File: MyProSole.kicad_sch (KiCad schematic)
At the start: 15 parts, among them J1 Conn_01x07_Socket_XIAO_ESP32C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, J2 XIAO_ESP32C3, J3 i2c-bus, J4 FSR1, J5 FSR2, J6 FSR3, J7 Conn_01x06

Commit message: Fix ERC
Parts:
- removed J4: FSR1, symbol Connector_Generic:Conn_01x02
- added J8: FSR3, symbol Connector_Generic:Conn_01x02
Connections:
- net +3.3V: no longer J5.1 (Pin_1), J6.1 (Pin_1)
- net GND: now also J5.2 (Pin_2), J6.2 (Pin_2), J8.2 (Pin_2)
- net FSR1_ADC renamed FSR1_Input
- net FSR1_Input: now also J6.1 (Pin_1); no longer J6.2 (Pin_2)
- net FSR2_ADC renamed FSR2_Input
- net FSR2_Input: now also J5.1 (Pin_1); no longer J5.2 (Pin_2)
- net FSR3_ADC renamed FSR3_Input
- net FSR3_Input: now also J8.1 (Pin_1)
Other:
- moved on the sheet: C1, D1, J1, J3, J5, J7, R1, TP1

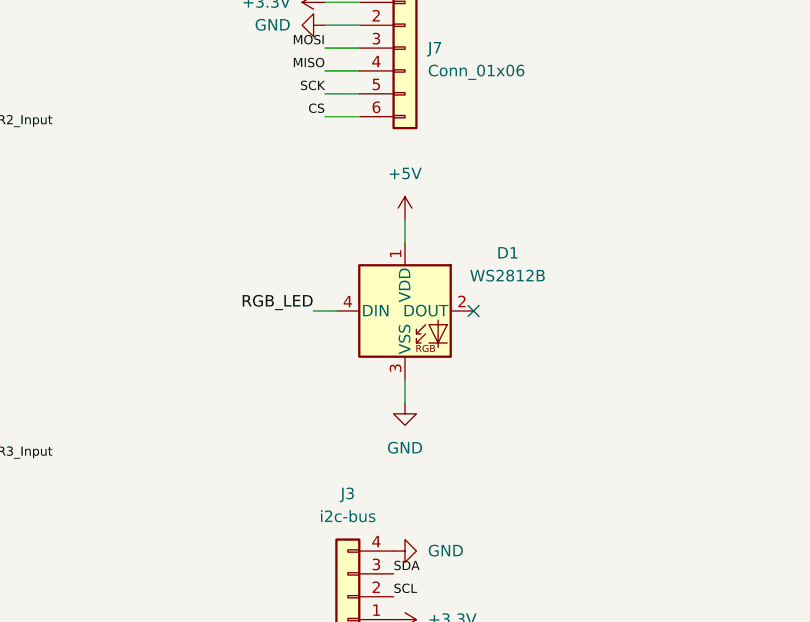
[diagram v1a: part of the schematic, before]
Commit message: Only some designed changes
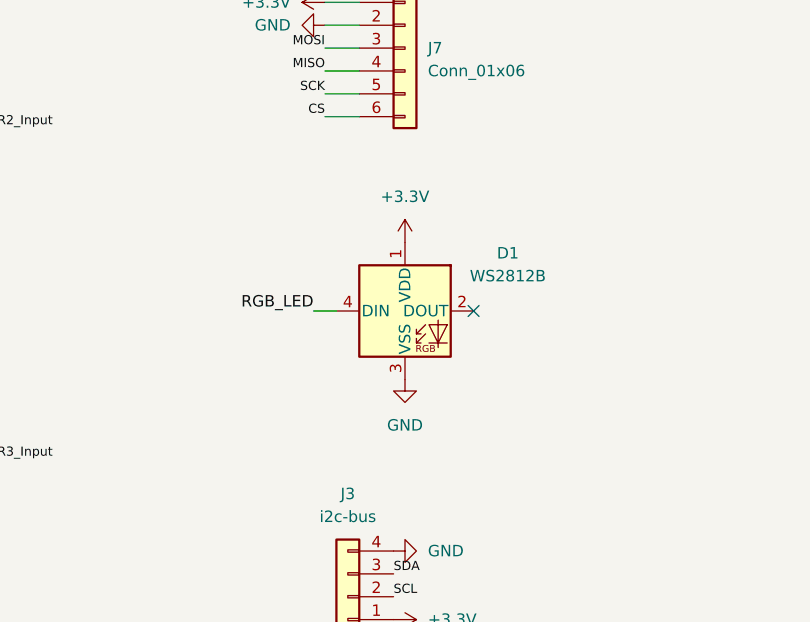
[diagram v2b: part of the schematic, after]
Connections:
- net +3.3V: now also D1.1 (VDD)
- net +5V: no longer D1.1 (VDD)
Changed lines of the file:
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@@
-	(wire
-		(pts
-			(xy 83.82 74.93) (xy 83.82 77.47)
-		)
-		(stroke
-			(width 0)
-			(type default)
-		)
-	)
 	(wire
 		(pts
@@
 		(pts
 			(xy 29.21 92.71) (xy 29.21 99.06)
-		)
-		(stroke
-			(width 0)
-			(type default)
-		)
-	)
-	(wire
-		(pts
-			(xy 83.82 92.71) (xy 83.82 95.25)
 		)
 		(stroke
@@
 	)
 	(symbol
+		(lib_id "power:+3.3V")
+		(at 83.82 77.47 0)
+		(unit 1)
+		(exclude_from_sim no)
+		(in_bom yes)
+		(on_board yes)
+		(dnp no)
+		(fields_autoplaced yes)
+		(property "Reference" "#PWR09"
+			(at 83.82 81.28 0)
+			(effects
+				(font
+					(size 1.27 1.27)
+				)
+				(hide yes)
+			)
+		)
+		(property "Value" "+3.3V"
+			(at 83.82 72.39 0)
+			(effects
+				(font
+					(size 1.27 1.27)
+				)
+			)
+		)
+		(property "Footprint" ""
+			(at 83.82 77.47 0)
+			(effects
+				(font
+					(size 1.27 1.27)
+				)
+				(hide yes)
+			)
+		)
+		(property "Datasheet" ""
+			(at 83.82 77.47 0)
+			(effects
+				(font
+					(size 1.27 1.27)
+				)
+				(hide yes)
+			)
+		)
+		(property "Description" "Power symbol creates a global label with name \"+3.3V\""
+			(at 83.82 77.47 0)
+			(effects
+				(font
+					(size 1.27 1.27)
+				)
+				(hide yes)
+			)
+		)
+		(pin "1"
+		)
+		(instances
+			(project ""
+				(path "/387d8c27-351f-4ca1-8104-be77ff5eb18f"
+					(reference "#PWR09")
+					(unit 1)
+				)
+			)
+		)
+	)
+	(symbol
 		(lib_id "Device:R_Small")
 		(at 31.75 107.95 180)
@@
 				(path "/387d8c27-351f-4ca1-8104-be77ff5eb18f"
 					(reference "R3")
-					(unit 1)
-				)
-			)
-		)
-	)
-	(symbol
-		(lib_id "power:GND")
-		(at 83.82 95.25 0)
-		(unit 1)
-		(exclude_from_sim no)
-		(in_bom yes)
-		(on_board yes)
-		(dnp no)
-		(fields_autoplaced yes)
-		(property "Reference" "#PWR011"
-			(at 83.82 101.6 0)
-			(effects
-				(font
-					(size 1.27 1.27)
-				)
-				(hide yes)
-			)
-		)
-		(property "Value" "GND"
-			(at 83.82 100.33 0)
-			(effects
-				(font
-					(size 1.27 1.27)
-				)
-			)
-		)
-		(property "Footprint" ""
-			(at 83.82 95.25 0)
-			(effects
-				(font
-					(size 1.27 1.27)
-				)
-				(hide yes)
-			)
-		)
-		(property "Datasheet" ""
-			(at 83.82 95.25 0)
-			(effects
-				(font
-					(size 1.27 1.27)
-				)
-				(hide yes)
-			)
-		)
-		(property "Description" "Power symbol creates a global label with name \"GND\" , ground"
-			(at 83.82 95.25 0)
-			(effects
-				(font
-					(size 1.27 1.27)
-				)
-				(hide yes)
-			)
-		)
-		(pin "1"
-		)
-		(instances
-			(project ""
-				(path "/387d8c27-351f-4ca1-8104-be77ff5eb18f"
-					(reference "#PWR011")
 					(unit 1)
 				)
@@
 	)
 	(symbol
-		(lib_id "power:+5V")
-		(at 83.82 74.93 0)
-		(unit 1)
-		(exclude_from_sim no)
-		(in_bom yes)
-		(on_board yes)
-		(dnp no)
-		(fields_autoplaced yes)
-		(property "Reference" "#PWR010"
-			(at 83.82 78.74 0)
-			(effects
-				(font
-					(size 1.27 1.27)
-				)
-				(hide yes)
-			)
-		)
-		(property "Value" "+5V"
-			(at 83.82 69.85 0)
-			(effects
-				(font
-					(size 1.27 1.27)
-				)
-			)
-		)
-		(property "Footprint" ""
-			(at 83.82 74.93 0)
-			(effects
-				(font
-					(size 1.27 1.27)
-				)
-				(hide yes)
-			)
-		)
-		(property "Datasheet" ""
-			(at 83.82 74.93 0)
-			(effects
-				(font
-					(size 1.27 1.27)
-				)
-				(hide yes)
-			)
-		)
-		(property "Description" "Power symbol creates a global label with name \"+5V\""
-			(at 83.82 74.93 0)
-			(effects
-				(font
-					(size 1.27 1.27)
-				)
-				(hide yes)
-			)
-		)
-		(pin "1"
-		)
-		(instances
-			(project ""
-				(path "/387d8c27-351f-4ca1-8104-be77ff5eb18f"
-					(reference "#PWR010")
-					(unit 1)
-				)
-			)
-		)
-	)
-	(symbol
 		(lib_id "MyProSoleLib:Conn_01x07_Socket_XIAO_ESP32C3_Left")
 		(at 73.66 34.29 0)
@@
 					(unit 1)
 				)
+			)
+		)
+	)
+	(symbol
+		(lib_id "power:GND")
+		(at 83.82 92.71 0)
+		(unit 1)
+		(exclude_from_sim no)
+		(in_bom yes)
+		(on_board yes)
+		(dnp no)
+		(fields_autoplaced yes)
+		(property "Reference" "#PWR010"
+			(at 83.82 99.06 0)
+			(effects
+				(font
+					(size 1.27 1.27)
+				)
+				(hide yes)
+			)
+		)
+		(property "Value" "GND"
+			(at 83.82 97.79 0)
+			(effects
+				(font
+					(size 1.27 1.27)
+				)
+			)
+		)
+		(property "Footprint" ""
+			(at 83.82 92.71 0)
+			(effects
+				(font
+					(size 1.27 1.27)
+				)
+				(hide yes)
+			)
+		)
+		(property "Datasheet" ""
+			(at 83.82 92.71 0)
+			(effects
+				(font
+					(size 1.27 1.27)
+				)
+				(hide yes)
+			)
+		)
+		(property "Description" "Power symbol creates a global label with name \"GND\" , ground"
+			(at 83.82 92.71 0)
+			(effects
+				(font
+					(size 1.27 1.27)
+				)
+				(hide yes)
+			)
+		)
+		(pin "1"
+		)
+		(instances
+			(project ""
+				(path "/387d8c27-351f-4ca1-8104-be77ff5eb18f"
+					(reference "#PWR010")
+					(unit 1)
+				)

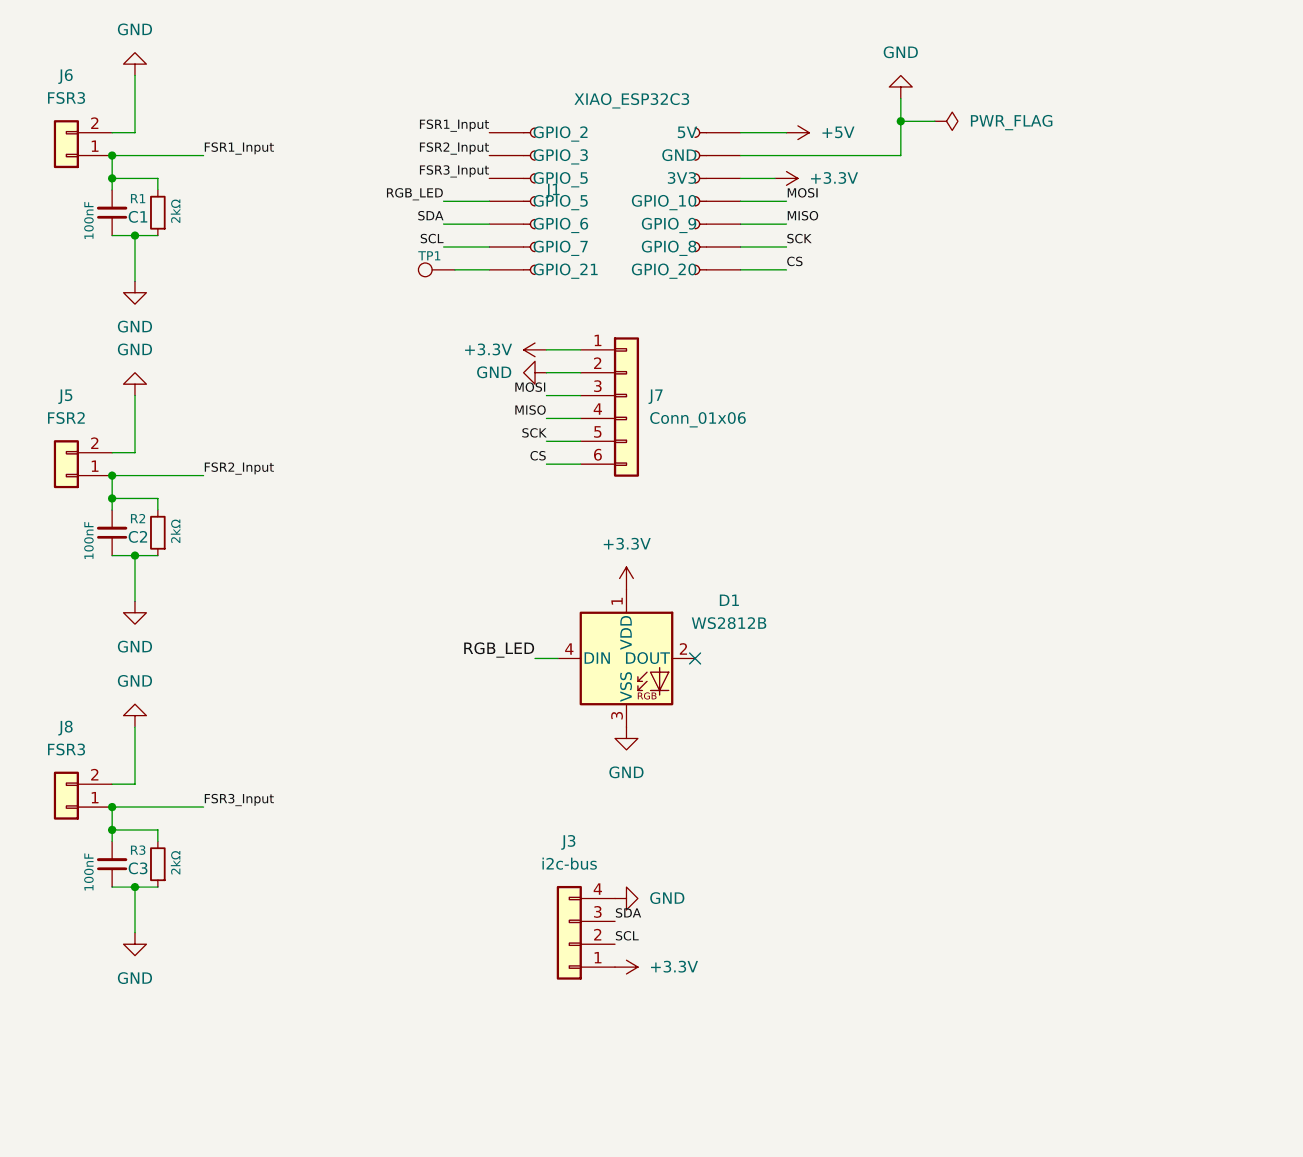
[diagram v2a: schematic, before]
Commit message: Added 5V led, Helper Socket for SD_Card & Footprints Added
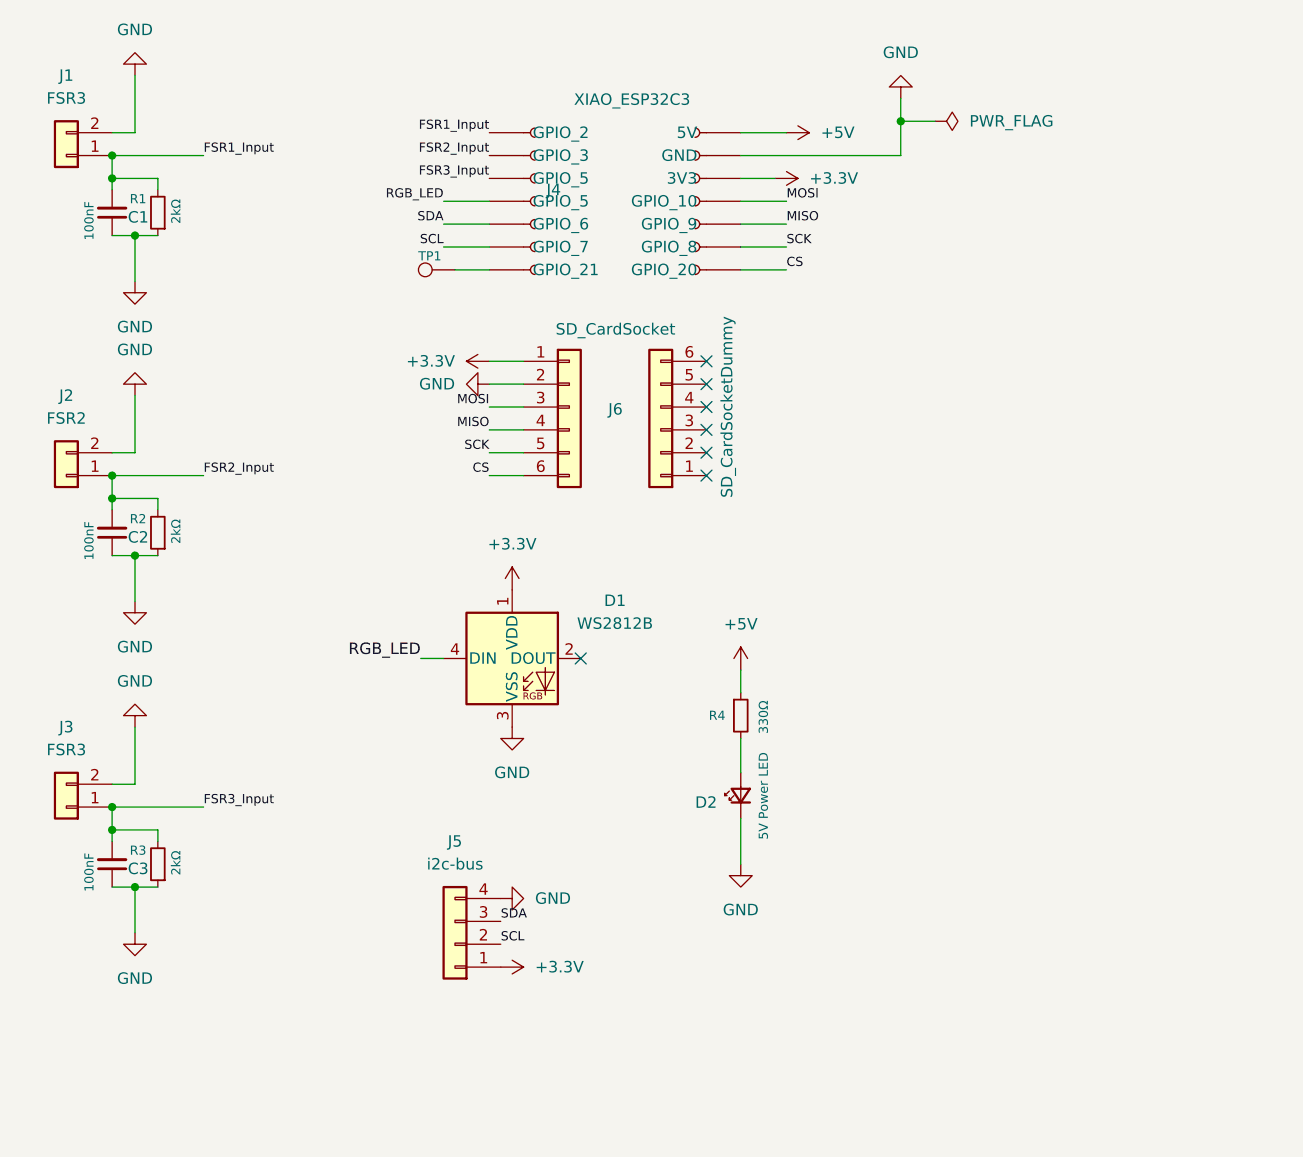
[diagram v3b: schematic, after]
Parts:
- added D2: 5V Power LED, LED_SMD:LED_miniPLCC_2315_Handsoldering, symbol Device:LED_Small
- added J8: SD_CardSocketDummy, Connector_PinSocket_2.54mm:PinSocket_1x06_P2.54mm_Vertical, symbol Connector_Generic:Conn_01x06
- added R4: 330Ω, Resistor_SMD:R_0805_2012Metric_Pad1.20x1.40mm_HandSolder, symbol Device:R_Small
- C1, C2, C3: footprint (none) -> Capacitor_SMD:C_0805_2012Metric_Pad1.18x1.45mm_HandSolder
- J1: renamed from J6; footprint (none) -> Connector_JST:JST_XH_B2B-XH-AM_1x02_P2.50mm_Vertical
- J2: renamed from J5; footprint (none) -> Connector_JST:JST_XH_B2B-XH-AM_1x02_P2.50mm_Vertical
- J3: renamed from J8; footprint (none) -> Connector_JST:JST_XH_B2B-XH-AM_1x02_P2.50mm_Vertical
- J4: renamed from J1; footprint (none) -> Connector_PinSocket_2.54mm:PinSocket_1x07_P2.54mm_Vertical
- J5: renamed from J3; footprint (none) -> Connector_JST:JST_XH_B2B-XH-AM_1x02_P2.50mm_Vertical
- J6: renamed from J7; value Conn_01x06 -> SD_CardSocket; footprint (none) -> Connector_PinSocket_2.54mm:PinSocket_1x06_P2.54mm_Vertical
- J7: renamed from J2; footprint (none) -> Connector_PinSocket_2.54mm:PinSocket_1x07_P2.54mm_Vertical
- R1, R2, R3: footprint (none) -> Resistor_SMD:R_0805_2012Metric_Pad1.20x1.40mm_HandSolder
- TP1: footprint (none) -> TestPoint:TestPoint_Pad_2.0x2.0mm
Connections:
- net +5V: now also R4.1
- net GND: now also D2.1 (K)
- new net: D2.2 (A), R4.2
- no-connect marks 1 -> 7
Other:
- moved on the sheet: D1, J5, J6

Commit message: First Step for Layout
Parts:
- J5: footprint Connector_JST:JST_XH_B2B-XH-AM_1x02_P2.50mm_Vertical -> Connector_JST:JST_XH_B4B-XH-AM_1x04_P2.50mm_Vertical
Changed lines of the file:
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@@
 			)
 		)
-		(property "Footprint" "Connector_JST:JST_XH_B2B-XH-AM_1x02_P2.50mm_Vertical"
+		(property "Footprint" "Connector_JST:JST_XH_B4B-XH-AM_1x04_P2.50mm_Vertical"
 			(at 64.77 116.84 0)
 			(effects

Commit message: almost ready for review
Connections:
- net +3.3V: now also J1.2 (Pin_2), J2.2 (Pin_2), J3.2 (Pin_2)
- net GND: no longer J1.2 (Pin_2), J2.2 (Pin_2), J3.2 (Pin_2)
- net SCL: now also J5.3 (Pin_3); no longer J5.2 (Pin_2)
- net SDA: now also J5.2 (Pin_2); no longer J5.3 (Pin_3)
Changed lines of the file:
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@@
-		)
-	)
-	(label "SCL"
-		(at 69.85 116.84 0)
-		(effects
-			(font
-				(size 1.016 1.016)
-			)
-			(justify left bottom)
 		)
 	)
@@
 		)
 	)
-	(label "SDA"
-		(at 69.85 114.3 0)
-		(effects
-			(font
-				(size 1.016 1.016)
-			)
-			(justify left bottom)
-		)
-	)
 	(label "MISO"
 		(at 68.58 59.69 180)
@@
 		)
 	)
+	(label "SCL"
+		(at 69.85 114.3 0)
+		(effects
+			(font
+				(size 1.016 1.016)
+			)
+			(justify left bottom)
+		)
+	)
 	(label "MOSI"
 		(at 68.58 57.15 180)
@@
 	)
 	(label "SDA"
+		(at 69.85 116.84 0)
+		(effects
+			(font
+				(size 1.016 1.016)
+			)
+			(justify left bottom)
+		)
+	)
+	(label "SDA"
 		(at 63.5 36.83 180)
 		(effects
@@
 	)
 	(symbol
+		(lib_id "power:+3.3V")
+		(at 29.21 20.32 0)
+		(unit 1)
+		(exclude_from_sim no)
+		(in_bom yes)
+		(on_board yes)
+		(dnp no)
+		(fields_autoplaced yes)
+		(property "Reference" "#PWR01"
+			(at 29.21 24.13 0)
+			(effects
+				(font
+					(size 1.27 1.27)
+				)
+				(hide yes)
+			)
+		)
+		(property "Value" "+3.3V"
+			(at 29.21 15.24 0)
+			(effects
+				(font
+					(size 1.27 1.27)
+				)
+			)
+		)
+		(property "Footprint" ""
+			(at 29.21 20.32 0)
+			(effects
+				(font
+					(size 1.27 1.27)
+				)
+				(hide yes)
+			)
+		)
+		(property "Datasheet" ""
+			(at 29.21 20.32 0)
+			(effects
+				(font
+					(size 1.27 1.27)
+				)
+				(hide yes)
+			)
+		)
+		(property "Description" "Power symbol creates a global label with name \"+3.3V\""
+			(at 29.21 20.32 0)
+			(effects
+				(font
+					(size 1.27 1.27)
+				)
+				(hide yes)
+			)
+		)
+		(pin "1"
+		)
+		(instances
+			(project ""
+				(path "/387d8c27-351f-4ca1-8104-be77ff5eb18f"
+					(reference "#PWR01")
+					(unit 1)
+				)
+			)
+		)
+	)
+	(symbol
 		(lib_id "Device:R_Small")
 		(at 31.75 35.56 180)
@@
 	)
 	(symbol
-		(lib_id "power:GND")
-		(at 29.21 20.32 180)
-		(unit 1)
-		(exclude_from_sim no)
-		(in_bom yes)
-		(on_board yes)
-		(dnp no)
-		(fields_autoplaced yes)
-		(property "Reference" "#PWR01"
-			(at 29.21 13.97 0)
-			(effects
-				(font
-					(size 1.27 1.27)
-				)
-				(hide yes)
-			)
-		)
-		(property "Value" "GND"
-			(at 29.21 15.24 0)
-			(effects
-				(font
-					(size 1.27 1.27)
-				)
-			)
-		)
-		(property "Footprint" ""
-			(at 29.21 20.32 0)
-			(effects
-				(font
-					(size 1.27 1.27)
-				)
-				(hide yes)
-			)
-		)
-		(property "Datasheet" ""
-			(at 29.21 20.32 0)
-			(effects
-				(font
-					(size 1.27 1.27)
-				)
-				(hide yes)
-			)
-		)
-		(property "Description" "Power symbol creates a global label with name \"GND\" , ground"
-			(at 29.21 20.32 0)
-			(effects
-				(font
-					(size 1.27 1.27)
-				)
-				(hide yes)
-			)
-		)
-		(pin "1"
-		)
-		(instances
-			(project ""
-				(path "/387d8c27-351f-4ca1-8104-be77ff5eb18f"
-					(reference "#PWR01")
-					(unit 1)
-				)
-			)
-		)
-	)
-	(symbol
 		(lib_id "Connector_Generic:Conn_01x02")
 		(at 21.59 101.6 180)
@@
 	)
 	(symbol
-		(lib_id "power:GND")
-		(at 29.21 92.71 180)
+		(lib_id "power:+3.3V")
+		(at 29.21 92.71 0)
 		(unit 1)
 		(exclude_from_sim no)
@@
 		(fields_autoplaced yes)
 		(property "Reference" "#PWR05"
-			(at 29.21 86.36 0)
-			(effects
-				(font
-					(size 1.27 1.27)
-				)
-				(hide yes)
-			)
-		)
-		(property "Value" "GND"
+			(at 29.21 96.52 0)
+			(effects
+				(font
+					(size 1.27 1.27)
+				)
+				(hide yes)
+			)
+		)
+		(property "Value" "+3.3V"
 			(at 29.21 87.63 0)
 			(effects
@@
 			)
 		)
-		(property "Description" "Power symbol creates a global label with name \"GND\" , ground"
+		(property "Description" "Power symbol creates a global label with name \"+3.3V\""
 			(at 29.21 92.71 0)
 			(effects
@@
 		)
 		(instances
-			(project ""
+			(project "MyProSole"
 				(path "/387d8c27-351f-4ca1-8104-be77ff5eb18f"
 					(reference "#PWR05")
@@
 	)
 	(symbol
+		(lib_id "power:+3.3V")
+		(at 29.21 55.88 0)
+		(unit 1)
+		(exclude_from_sim no)
+		(in_bom yes)
+		(on_board yes)
+		(dnp no)
+		(fields_autoplaced yes)
+		(property "Reference" "#PWR03"
+			(at 29.21 59.69 0)
+			(effects
+				(font
+					(size 1.27 1.27)
+				)
+				(hide yes)
+			)
+		)
+		(property "Value" "+3.3V"
+			(at 29.21 50.8 0)
+			(effects
+				(font
+					(size 1.27 1.27)
+				)
+			)
+		)
+		(property "Footprint" ""
+			(at 29.21 55.88 0)
+			(effects
+				(font
+					(size 1.27 1.27)
+				)
+				(hide yes)
+			)
+		)
+		(property "Datasheet" ""
+			(at 29.21 55.88 0)
+			(effects
+				(font
+					(size 1.27 1.27)
+				)
+				(hide yes)
+			)
+		)
+		(property "Description" "Power symbol creates a global label with name \"+3.3V\""
+			(at 29.21 55.88 0)
+			(effects
+				(font
+					(size 1.27 1.27)
+				)
+				(hide yes)
+			)
+		)
+		(pin "1"
+		)
+		(instances
+			(project "MyProSole"
+				(path "/387d8c27-351f-4ca1-8104-be77ff5eb18f"
+					(reference "#PWR03")
+					(unit 1)
+				)
+			)
+		)
+	)
+	(symbol
 		(lib_id "Connector_Generic:Conn_01x02")
 		(at 21.59 29.21 180)
@@
 					(unit 1)
 				)
-			)
-		)
-	)
-	(symbol
-		(lib_id "power:GND")
-		(at 29.21 55.88 180)
-		(unit 1)
-		(exclude_from_sim no)
-		(in_bom yes)
-		(on_board yes)
-		(dnp no)
-		(fields_autoplaced yes)
-		(property "Reference" "#PWR03"
-			(at 29.21 49.53 0)
-			(effects
-				(font
-					(size 1.27 1.27)
-				)
-				(hide yes)
-			)
-		)
-		(property "Value" "GND"
-			(at 29.21 50.8 0)
-			(effects
-				(font
-					(size 1.27 1.27)
-				)
-			)
-		)
-		(property "Footprint" ""
-			(at 29.21 55.88 0)
-			(effects
-				(font
-					(size 1.27 1.27)
-				)
-				(hide yes)
-			)
-		)
-		(property "Datasheet" ""
-			(at 29.21 55.88 0)
-			(effects
-				(font
-					(size 1.27 1.27)
-				)
-				(hide yes)
-			)
-		)
-		(property "Description" "Power symbol creates a global label with name \"GND\" , ground"
-			(at 29.21 55.88 0)
-			(effects
-				(font
-					(size 1.27 1.27)
-				)
-				(hide yes)
-			)
-		)
-		(pin "1"
-		)
-		(instances
-			(project ""
-				(path "/387d8c27-351f-4ca1-8104-be77ff5eb18f"
-					(reference "#PWR03")
-					(unit 1)
-				)

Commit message: first prototyp versions
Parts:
- added C4: 10uF, Capacitor_SMD:C_0805_2012Metric_Pad1.18x1.45mm_HandSolder, symbol Device:C_Small
- added D3, D4, D5: ESD5Zxx, Diode_SMD:D_SOD-523, symbol Diode:ESD5Zxx
- C1, C2, C3: value 100nF -> 10nF
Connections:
- net +3.3V: now also C4.2
- net FSR1_Input: now also D3.1 (K)
- net FSR2_Input: now also D4.1 (K)
- net FSR3_Input: now also D5.1 (K)
- net GND: now also C4.1, D3.2 (A), D4.2 (A), D5.2 (A)
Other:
- moved on the sheet: C1, R1
